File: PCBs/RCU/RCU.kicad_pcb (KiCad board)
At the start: 2 copper layers, 155 parts, among them J100 Conn_01x02, J200 USB_C_Receptacle_USB2.0, J201 Conn_01x05, J300 Right_Motor_Screw_Terminal, J301 Right_Encoder_Conn, J302 Left_Motor_Screw_Terminal, J303 Left_Encoder_Conn, J400 USB_C_Receptacle_USB2.0, Q400 2N7002NXAKR (NMOS), Q401 2N7002NXAKR (NMOS), Q402 BSS84AK,215 (PMOS), Q403 2N7002NXAKR (NMOS), SW201 SW_Push, SW400 SW_Push, SW401 SW_SPDT, U100 AP63203WU, U101 AZ1117-3.3, U102 AP63203WU, U103 LM2576S-ADJ, U200 STM32G0B1CBT6, U201 USBLC6-2SC6, U300 OPA320, U301 DRV8876, U302 OPA320, U303 DRV8876, U400 USBLC6-2SC6, U401 CH340C, U402 ESP32-MINI-1, U403 DG2788ADN-T1-GE4, U500 APDS-9306-065, U501 LSM6DS3, U502 SHT30-DIS, U600 ADC121C027CIMK/NOPB, U601 OPA320, U602 ADC121C027CIMK/NOPB, U603 OPA320, U700 SST26VF032BT-104I/SM, Y200 16MHz

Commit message: Roughly sectioned modules
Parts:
- removed C113: 100nF, Capacitor_SMD:C_0603_1608Metric
- removed C114, C115: 22uF, Capacitor_SMD:C_0603_1608Metric
- removed C116: 100uF, Capacitor_THT:CP_Radial_D5.0mm_P2.50mm
- removed C117: 1000uF, Capacitor_THT:CP_Radial_D5.0mm_P2.50mm
- removed D105: 1N5822, Diode_THT:D_DO-201AD_P15.24mm_Horizontal
- removed L104: 15uH, Inductor_SMD:L_0603_1608Metric
- removed L105: 68uH, Inductor_SMD:L_12x12mm_H6mm
- removed U103: LM2576S-ADJ, Package_TO_SOT_SMD:TO-263-5_TabPin3
- added C101: 100uF, Capacitor_THT:CP_Radial_D5.0mm_P2.50mm, F.Cu at (45.4, 123.2)
- added L100: 68uH, Inductor_SMD:L_12x12mm_H6mm, F.Cu at (30.4, 135.2)
- C102: value 10uF -> 1000uF; footprint Capacitor_SMD:C_0603_1608Metric -> Capacitor_THT:CP_Radial_D5.0mm_P2.50mm
- C103: value 100nF -> 10uF
- C104: value 22uF -> 100nF
- C106, C110: value 1uF -> 22uF
- C108: value 22uF -> 1uF
- C112: value 10uF -> 1uF
- D100: value SM5817 -> 1N5822; footprint Schottky_Diode:SODFL3719X135N -> Diode_THT:D_DO-201AD_P15.24mm_Horizontal
- L101: value 82uH -> 15uH
- R100: value 5R -> 8.9k
- R101: value 8.9k -> 1.5k
- R102: value 1.5k -> 5R
- U100: value AP63203WU -> LM2576S-ADJ; footprint Package_TO_SOT_SMD:TSOT-23-6 -> Package_TO_SOT_SMD:TO-263-5_TabPin3
- U101: value AZ1117-3.3 -> AP63203WU; footprint Package_TO_SOT_SMD:TO-252-2 -> Package_TO_SOT_SMD:TSOT-23-6
- U102: value AP63203WU -> AZ1117-3.3; footprint Package_TO_SOT_SMD:TSOT-23-6 -> Package_TO_SOT_SMD:TO-252-2
- moved U101 252.6 mm to (89.9, -27.1)
- moved C102 236.1 mm to (15.4, 122.2)
- moved C108 215.7 mm to (47.2, 12.0)
- moved U102 213.9 mm to (89.0, 187.0)
- moved D101 185.1 mm to (39.0, 71.0)
- moved U100 179.9 mm to (31.1, 119.2)
- moved D100 177.4 mm to (23.8, 107.2)
- moved C107 175.9 mm to (35.7, 13.0), turned to 180 degrees
- moved C110 173.0 mm to (78.0, 187.0)
- moved R100 171.0 mm to (45.4, 112.2)
- moved D102 164.2 mm to (54.2, 9.00)
- moved L102 157.6 mm to (40.2, 9.00)
- moved C103 151.8 mm to (81.7, -27.1)
- moved C104 140.1 mm to (96.7, -27.1)
- moved C408 139.6 mm to (124.1, -39.0)
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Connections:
- C102 pad 1: VCOM -> +6V
- C103 pad 1: /[1] Power/BOOST_IN_104 -> VCOM
- C103 pad 2: /[1] Power/SWO_100 -> GND
- C104 pad 1: +3V3 -> /[1] Power/BOOST_IN_104
- C104 pad 2: GND -> /[1] Power/SWO_100
- C106 pad 1: /[1] Power/VBUS1 -> +3V3
- C107 pad 1: +5C -> /[1] Power/VBUS1
- C108 pad 1: /[1] Power/BATT_FILT -> +5C
- C109 pad 1: +3.3VA -> /[1] Power/BATT_FILT
- C110 pad 1: /[1] Power/VBUS2 -> +3.3VA
- C111 pad 1: +5F -> /[1] Power/VBUS2
- C112 pad 1: Net-(C112-Pad1) -> +5F
- C400 pad 1: +3.3VP -> +3V3
- C401 pad 1: +3.3VP -> +3V3
- C402 pad 1: +3.3VP -> +3V3
- C403 pad 1: +3.3VP -> +3V3
- C404 pad 1: +3.3VP -> +3V3
- C407 pad 1: +3.3VP -> +3V3
- C408 pad 1: +3.3VP -> +3V3
- D100 pad 1: VCOM -> /[1] Power/BUCK_OUT_104
- D100 pad 2: +BATT -> GND
- D101 pad 2: +5C -> +BATT
- D102 pad 1: Net-(C112-Pad1) -> VCOM
- D102 pad 2: VCOM -> +5C
- D104 pad 1: Net-(C112-Pad1) -> VCOM
- Q402 pad 1: +3.3VP -> +3V3
- R100 pad 1: VCOM -> /[1] Power/BUCK_FB_104
- R100 pad 2: /[1] Power/BATT_FILT -> +6V
- R101 pad 1: /[1] Power/BUCK_FB_104 -> GND
- R101 pad 2: +6V -> /[1] Power/BUCK_FB_104
- R102 pad 1: GND -> VCOM
- R102 pad 2: /[1] Power/BUCK_FB_104 -> /[1] Power/BATT_FILT
- R404 pad 2: +3.3VP -> +3V3
- R407 pad 1: +3.3VP -> +3V3
- U100 pad 1: +3V3 -> +BATT
- U100 pad 2: VCOM -> /[1] Power/BUCK_OUT_104
- U100 pad 3: VCOM -> GND
- U100 pad 4: GND -> /[1] Power/BUCK_FB_104
- U100 pad 5: /[1] Power/SWO_100 -> GND
- U101 pad 1: GND -> +3V3
- U101 pad 2: +3.3VA -> VCOM
- U101 pad 3: /[1] Power/BATT_FILT -> VCOM
- U102 pad 1: +3.3VP -> GND
- U102 pad 2: Net-(C112-Pad1) -> +3.3VA
- U102 pad 3: Net-(C112-Pad1) -> /[1] Power/BATT_FILT
- U401 pad 16: +3.3VP -> +3V3
- U401 pad 4: +3.3VP -> +3V3
- U402 pad 3: +3.3VP -> +3V3
- U403 pad 10: +3.3VP -> +3V3

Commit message: Added stackup - JLC7628
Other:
- copper layers 2 -> 4
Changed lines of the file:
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@@
 (kicad_pcb (version 20211014) (generator pcbnew)
   (general
-    (thickness 1.6)
+    (thickness 1.6062)
   )
   (paper "A4")
   (layers
     (0 "F.Cu" signal)
+    (1 "In1.Cu" power)
+    (2 "In2.Cu" power)
     (31 "B.Cu" signal)
     (32 "B.Adhes" user "B.Adhesive")
@@
   )
   (setup
+    (stackup
+      (layer "F.SilkS" (type "Top Silk Screen"))
+      (layer "F.Paste" (type "Top Solder Paste"))
+      (layer "F.Mask" (type "Top Solder Mask") (thickness 0.01))
+      (layer "F.Cu" (type "copper") (thickness 0.035))
+      (layer "dielectric 1" (type "prepreg") (thickness 0.2104) (material "FR4") (epsilon_r 4.4) (loss_tangent 0.02))
+      (layer "In1.Cu" (type "copper") (thickness 0.0152))
+      (layer "dielectric 2" (type "core") (thickness 1.065) (material "FR4") (epsilon_r 4.6) (loss_tangent 0.02))
+      (layer "In2.Cu" (type "copper") (thickness 0.0152))
+      (layer "dielectric 3" (type "prepreg") (thickness 0.2104) (material "FR4") (epsilon_r 4.4) (loss_tangent 0.02))
+      (layer "B.Cu" (type "copper") (thickness 0.035))
+      (layer "B.Mask" (type "Bottom Solder Mask") (thickness 0.01))
+      (layer "B.Paste" (type "Bottom Solder Paste"))
+      (layer "B.SilkS" (type "Bottom Silk Screen"))
+      (copper_finish "None")
+      (dielectric_constraints no)
+    )
     (pad_to_mask_clearance 0)
     (pcbplotparams

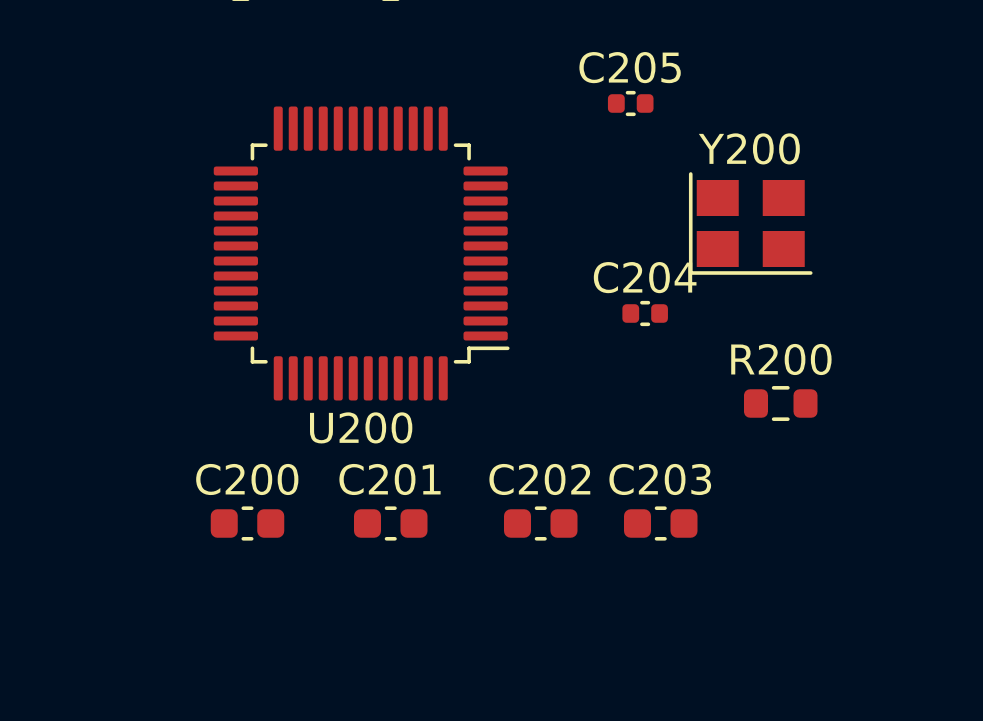
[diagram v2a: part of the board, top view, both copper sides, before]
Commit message: Changed filter caps for uC to 0402s
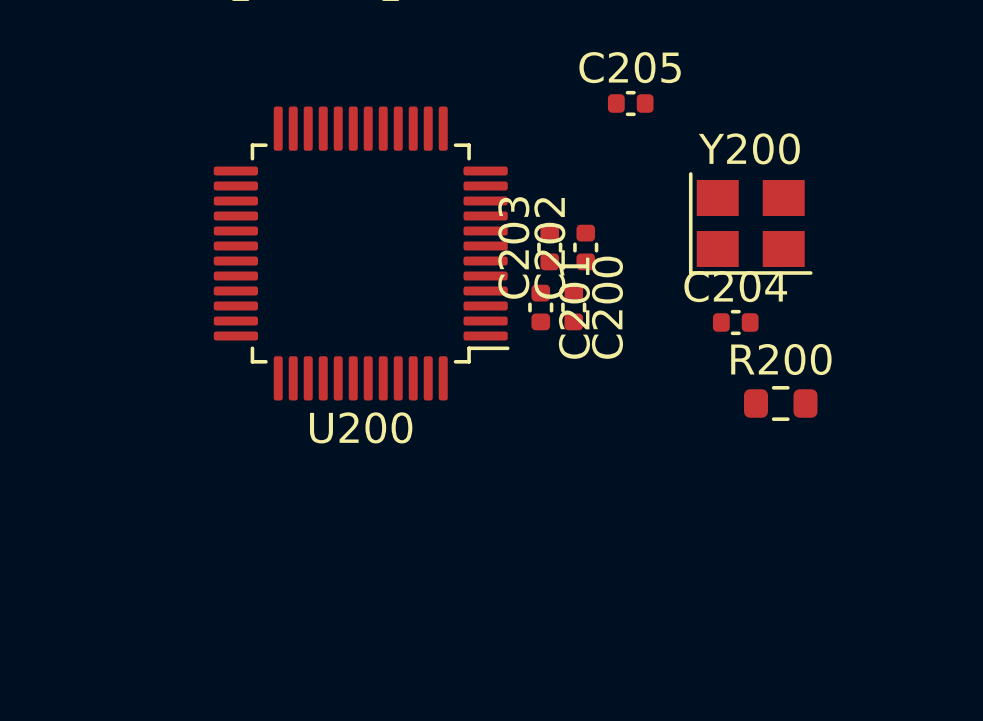
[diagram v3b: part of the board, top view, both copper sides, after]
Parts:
- C200, C201, C202, C203: footprint Capacitor_SMD:C_0603_1608Metric -> Capacitor_SMD:C_0402_1005Metric
- moved C200 13.0 mm to (144.1, 22.8), turned to -90 degrees
- moved C203 9.92 mm to (143.3, 20.8), turned to 90 degrees
- moved C202 9.32 mm to (144.5, 20.8), turned to 90 degrees
- moved C201 8.77 mm to (143.0, 22.8), turned to -90 degrees
- moved C204 3.03 mm to (149.5, 23.3)

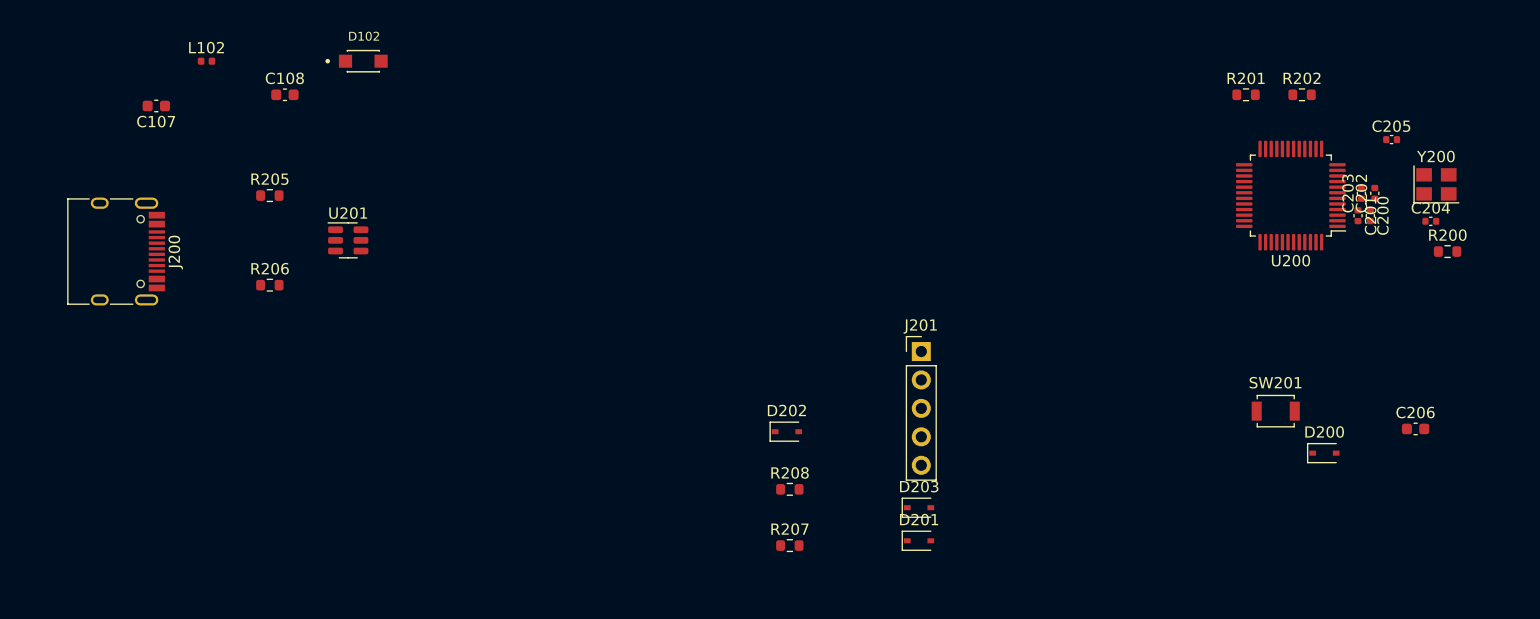
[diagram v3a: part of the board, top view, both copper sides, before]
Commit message: Finished mcu placement
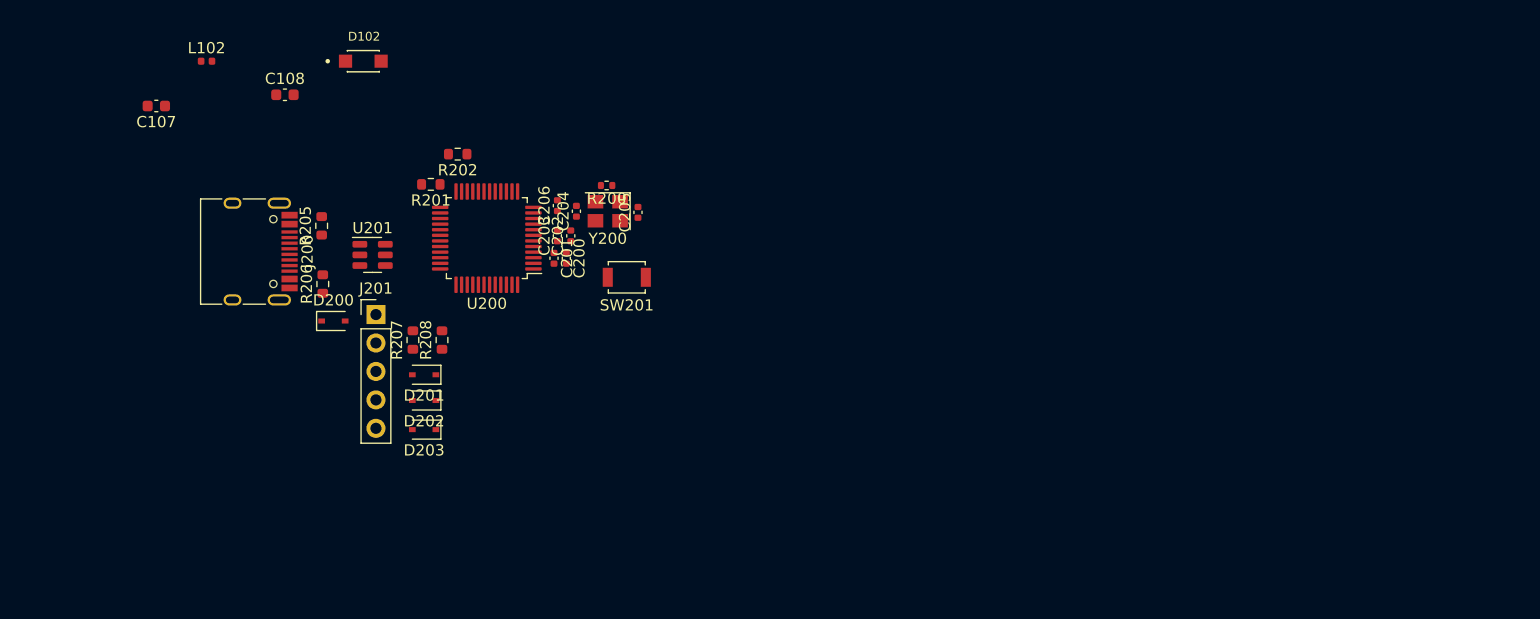
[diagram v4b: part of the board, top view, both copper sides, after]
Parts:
- C206: footprint Capacitor_SMD:C_0603_1608Metric -> Capacitor_SMD:C_0402_1005Metric
- R200: footprint Resistor_SMD:R_0603_1608Metric -> Resistor_SMD:R_0402_1005Metric
- moved D200 89.3 mm to (51.5, 32.2)
- moved C206 79.2 mm to (71.5, 21.9), turned to 90 degrees
- moved C204 76.3 mm to (73.2, 22.4), turned to 90 degrees
- moved R202 75.6 mm to (62.6, 17.3), turned to 180 degrees
- moved R200 75.3 mm to (75.9, 20.1), turned to 180 degrees
- moved Y200 74.0 mm to (76.0, 22.4), turned to 180 degrees
- moved R201 73.2 mm to (60.2, 20.0), turned to 180 degrees
- moved C203 71.9 mm to (71.5, 24.6)
- moved C200 71.9 mm to (72.3, 26.6)
- moved C201 71.9 mm to (71.2, 26.6)
- moved C202 71.9 mm to (72.7, 24.6)
- moved U200 71.9 mm to (65.2, 24.8)
- moved C205 67.6 mm to (78.7, 22.5), turned to 90 degrees
- moved SW201 59.2 mm to (77.7, 28.3), turned to 180 degrees
- moved J201 48.8 mm to (55.3, 31.6)
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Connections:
- D201 pad 2: /[2] Microcontroller/SWCLK -> /[2] Microcontroller/SWDIO
- D202 pad 2: /[2] Microcontroller/SWDIO -> /[2] Microcontroller/SWCLK
- J201 pad 3: /[2] Microcontroller/SWCLK -> /[2] Microcontroller/SWDIO
- J201 pad 4: /[2] Microcontroller/SWDIO -> /[2] Microcontroller/SWCLK
- R207 pad 1: /[2] Microcontroller/SWCLK -> /[2] Microcontroller/SWDIO
- R207 pad 2: /[2] Microcontroller/SWCLK_Pin -> /[2] Microcontroller/SWDIO_Pin
- R208 pad 1: /[2] Microcontroller/SWDIO -> /[2] Microcontroller/SWCLK
- R208 pad 2: /[2] Microcontroller/SWDIO_Pin -> /[2] Microcontroller/SWCLK_Pin

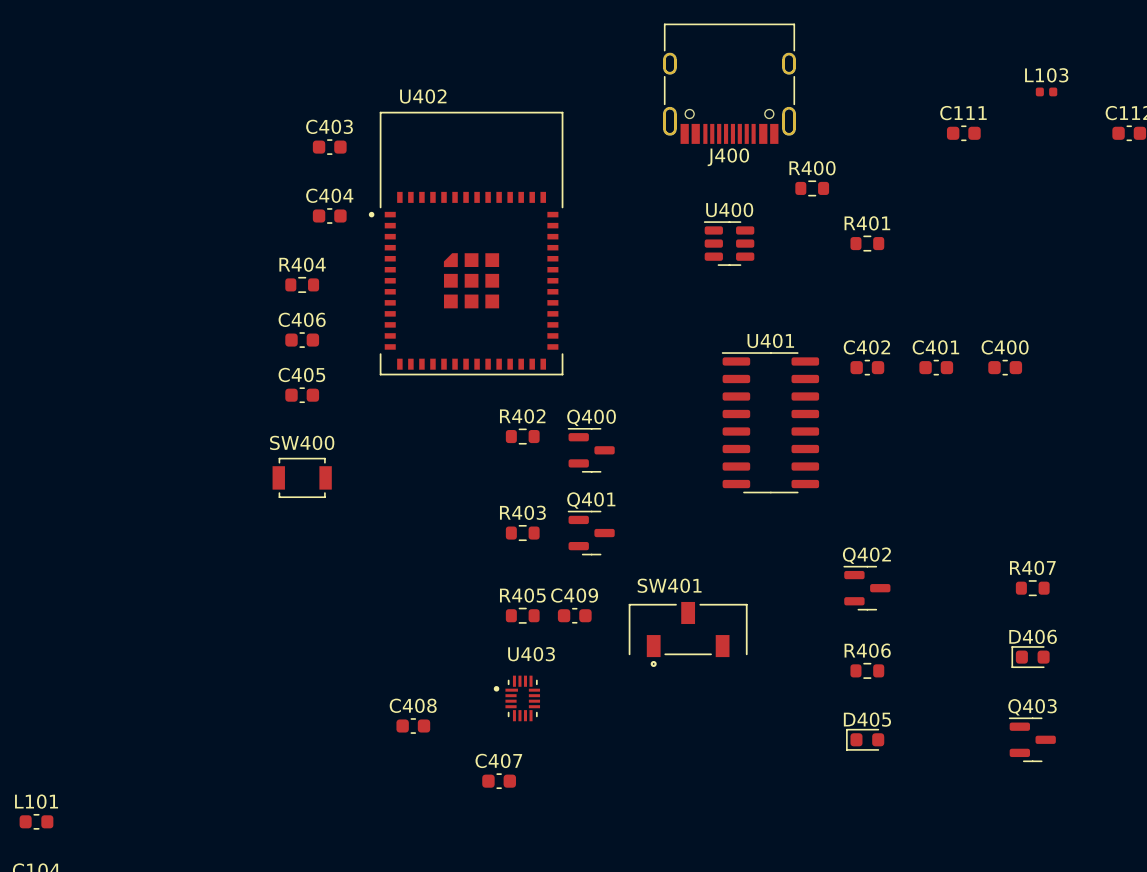
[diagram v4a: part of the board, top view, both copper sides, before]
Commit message: Organized Microcontroller and blutooth layout
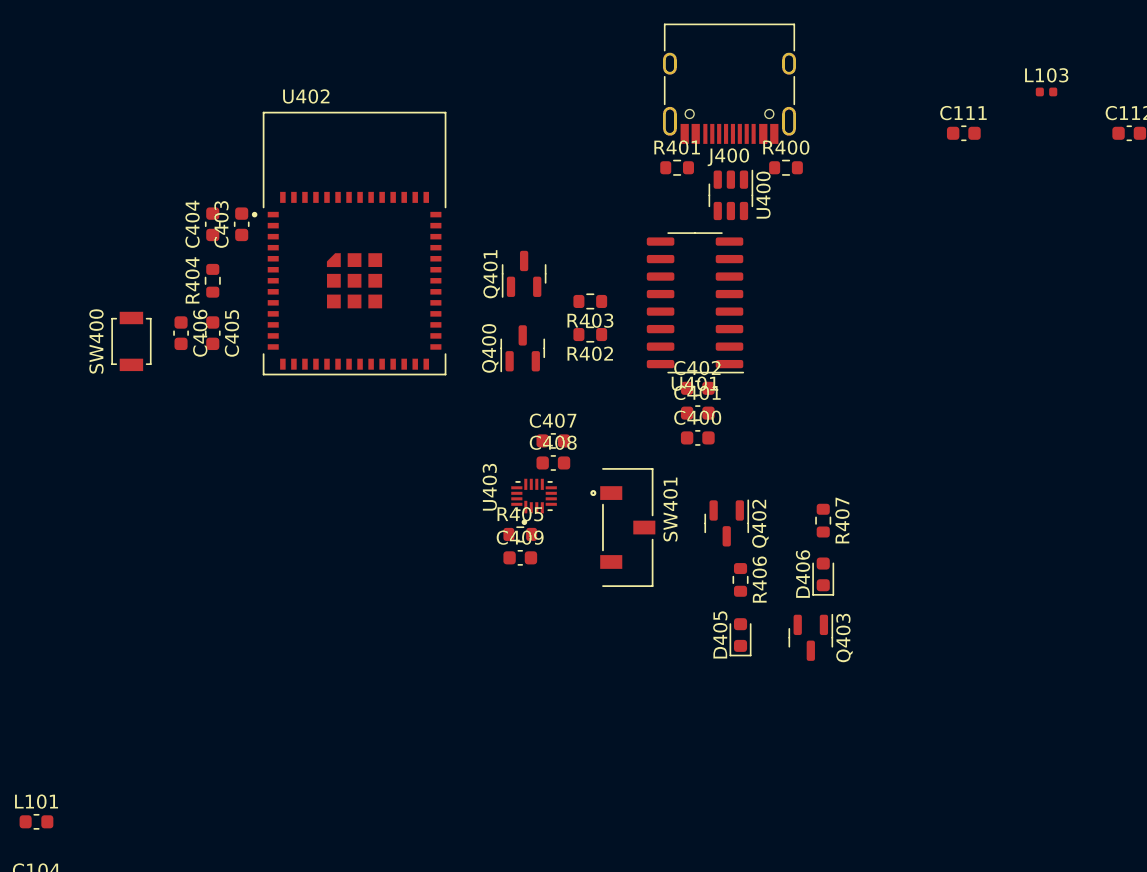
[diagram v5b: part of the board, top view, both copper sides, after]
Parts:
- moved C407 25.0 mm to (134.2, -59.7)
- moved C400 22.9 mm to (144.7, -59.9)
- moved C408 21.6 mm to (134.2, -58.1)
- moved Q401 19.4 mm to (132.1, -71.8), turned to 90 degrees
- moved Q403 17.7 mm to (152.9, -45.4), turned to -90 degrees
- moved C401 17.6 mm to (144.7, -61.7)
- moved R403 17.5 mm to (136.9, -69.8), turned to 180 degrees
- moved D406 16.3 mm to (153.8, -50.0), turned to 90 degrees
- moved R407 16.0 mm to (153.8, -53.9), turned to -90 degrees
- moved SW400 15.9 mm to (103.6, -66.9), turned to 90 degrees
- moved R401 14.9 mm to (143.2, -79.5)
- moved U403 14.7 mm to (132.8, -55.7), turned to 90 degrees
- moved C402 12.4 mm to (144.7, -63.5)
- moved D405 11.9 mm to (147.8, -45.6), turned to 90 degrees
- moved R406 11.3 mm to (147.8, -49.6), turned to -90 degrees
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
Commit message: Added 3d models and board outline on edge cuts layer
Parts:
- moved C102 170.8 mm to (-130.8, 210.6)
- moved L100 170.8 mm to (-115.8, 223.6)
- moved U100 170.8 mm to (-115.2, 207.6)
- moved C100 170.8 mm to (-115.2, 159.4)
- moved C101 170.8 mm to (-100.8, 211.6)
- moved D100 170.8 mm to (-122.4, 195.6)
- moved D101 170.8 mm to (-107.2, 159.4)
- moved J100 170.8 mm to (-124.2, 156.5)
- moved R100 170.8 mm to (-100.8, 200.6)
- moved R101 170.8 mm to (-96.8, 203.6)
- moved L103 128.5 mm to (122.3, 34.3)
- moved C112 128.1 mm to (124.3, 35.2), turned to -90 degrees
- moved C111 125.1 mm to (120.3, 35.2), turned to -90 degrees
- moved C401 115.8 mm to (114.2, 50.0)
- moved C402 115.8 mm to (114.2, 48.2)
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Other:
- board outline added: 99 x 139 mm

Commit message: Added motor driver footrpint and replaced diode 1N5822 with B340AE-13
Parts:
- D100: value 1N5822 -> B340; footprint Diode_THT:D_DO-201AD_P15.24mm_Horizontal -> Diode_SMD:D_SMC
- R300, R306: footprint Resistor_SMD:R_0603_1608Metric -> Resistor_SMD:R_0402_1005Metric
- moved C102 298.7 mm to (152.1, 114.8)
- moved J100 296.0 mm to (163.2, 85.8), turned to 90 degrees
- moved U100 292.6 mm to (157.8, 102.3)
- moved D100 284.4 mm to (144.4, 97.3), turned to 90 degrees
- moved C100 281.9 mm to (156.1, 82.9), turned to 90 degrees
- moved L100 281.6 mm to (141.8, 109.8), turned to -90 degrees
- moved C101 278.8 mm to (152.1, 94.4), turned to 90 degrees
- moved D101 271.5 mm to (154.7, 88.0)
- moved R101 266.9 mm to (153.0, 109.7), turned to 180 degrees
- moved R100 266.6 mm to (150.1, 110.3), turned to -90 degrees
- moved C307 27.1 mm to (81.0, 123.8), turned to 90 degrees
- moved C306 21.6 mm to (107.5, 122.0), turned to -90 degrees
- moved U302 19.6 mm to (84.1, 123.3), turned to 180 degrees
- moved D300 18.0 mm to (120.0, 104.5)
- moved D301 18.0 mm to (120.0, 108.5)
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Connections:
- U301 pad 17: (no net) -> GND
- U303 pad 17: (no net) -> GND
